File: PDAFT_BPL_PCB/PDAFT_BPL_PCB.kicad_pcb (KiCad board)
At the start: 2 copper layers, 63.4 x 87.5 mm, 18 parts

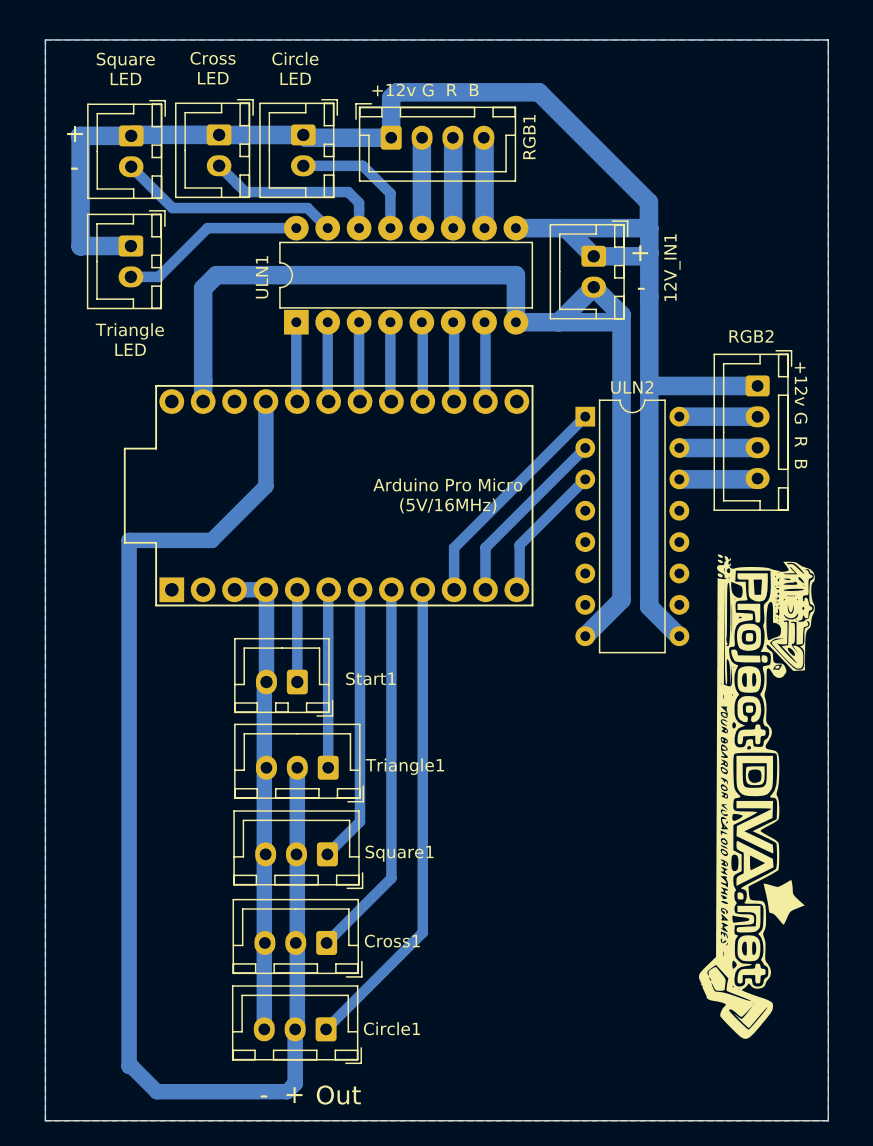
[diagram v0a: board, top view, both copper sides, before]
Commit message: Update PCB
Update PCB to make fast write to registers in interruptions when received LEDs data by UART
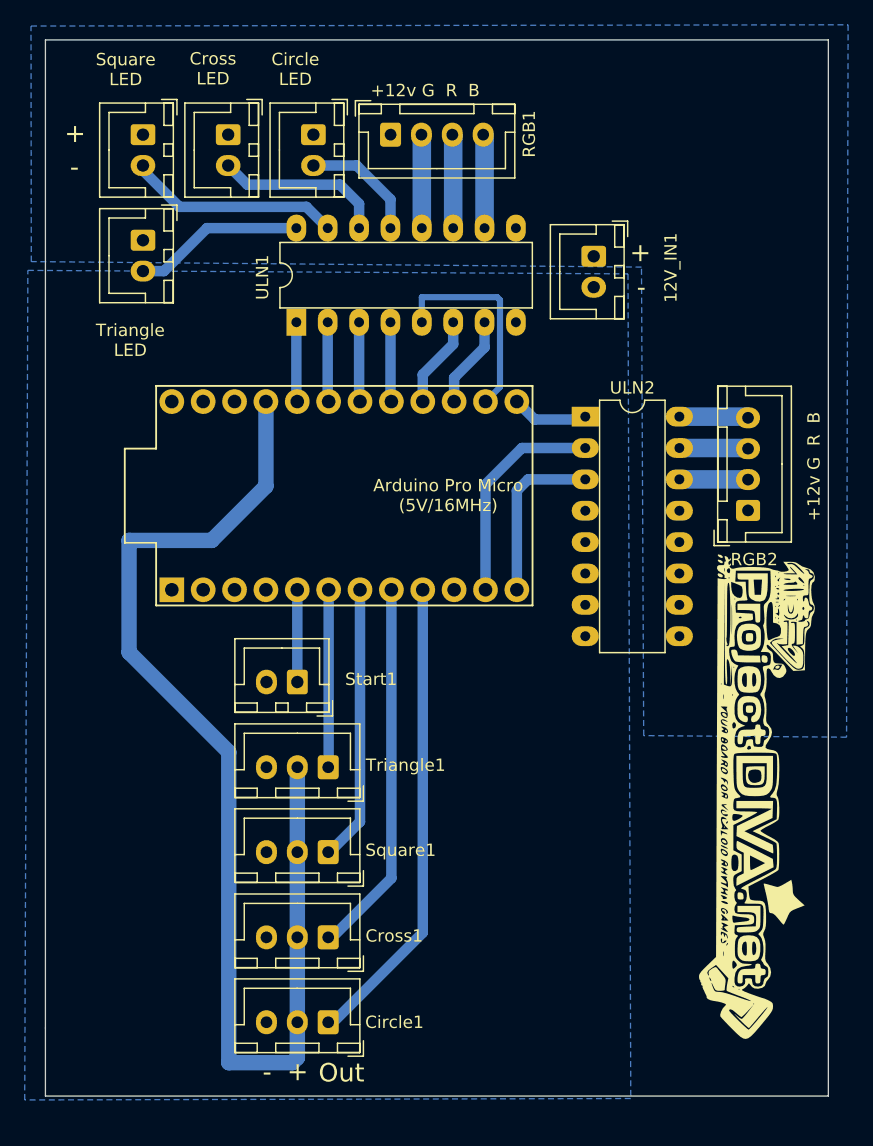
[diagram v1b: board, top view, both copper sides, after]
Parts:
- moved RGB2 10.1 mm to (158.5, 68.6), turned to 90 degrees
- moved G*** 2.63 mm to (153.6, 96.1)
- moved TRIANGLE_LED1 1.08 mm to (109.5, 46.7)
- moved SQUARE_LED1 0.96 mm to (109.5, 38.1)
- moved CIRCLE_LED1 0.82 mm to (123.3, 38.1)
- moved CROSS_LED1 0.74 mm to (116.4, 38.1)
- moved Circle1 0.60 mm to (124.5, 110.0)
- moved Cross1 0.47 mm to (124.5, 103.2)
- moved RGB1 0.25 mm to (129.6, 38.1)
- moved Square1 0.19 mm to (124.5, 96.2)
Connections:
- ProMicro1 pad 1: Net-(ProMicro1-Pad1) -> (no net)
- ProMicro1 pad 10: Net-(ProMicro1-Pad10) -> (no net)
- ProMicro1 pad 2: Net-(ProMicro1-Pad2) -> (no net)
- ProMicro1 pad 22: Net-(ProMicro1-Pad22) -> (no net)
- ProMicro1 pad 24: Net-(ProMicro1-Pad24) -> (no net)
- ULN1 pad 5: Net-(ProMicro1-Pad16) -> Net-(ProMicro1-Pad14)
- ULN1 pad 6: Net-(ProMicro1-Pad15) -> Net-(ProMicro1-Pad16)
- ULN1 pad 7: Net-(ProMicro1-Pad14) -> Net-(ProMicro1-Pad15)
- ULN2 pad 1: Net-(ProMicro1-Pad10) -> Net-(ProMicro1-Pad13)
- ULN2 pad 10: Net-(ULN2-Pad10) -> (no net)
- ULN2 pad 11: Net-(ULN2-Pad11) -> (no net)
- ULN2 pad 12: Net-(ULN2-Pad12) -> (no net)
- ULN2 pad 13: Net-(ULN2-Pad13) -> (no net)
- ULN2 pad 14: Net-(RGB2-Pad4) -> Net-(RGB2-Pad2)
- ULN2 pad 16: Net-(RGB2-Pad2) -> Net-(RGB2-Pad4)
- ULN2 pad 4: Net-(ULN2-Pad4) -> (no net)
- ULN2 pad 5: Net-(ULN2-Pad5) -> (no net)
- ULN2 pad 6: Net-(ULN2-Pad6) -> (no net)
- ULN2 pad 7: Net-(ULN2-Pad7) -> (no net)
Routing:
- net Net-(12V_IN1-Pad1): track 130.0 -> 0.00 mm
- net Net-(12V_IN1-Pad2): track 120.2 -> 0.31 mm
- net Net-(ProMicro1-Pad10): track 18.6 -> 0.00 mm
- net Net-(ProMicro1-Pad14): track 6.46 -> 17.3 mm
- net Net-(Circle1-Pad2): track 103.0 -> 94.8 mm
- net Net-(ProMicro1-Pad13): track 0.00 -> 6.24 mm
- net Net-(ProMicro1-Pad11): track 15.0 -> 17.8 mm
- net Net-(ProMicro1-Pad12): track 11.2 -> 13.9 mm
- net Net-(TRIANGLE_LED1-Pad2): track 15.1 -> 13.9 mm
- net Net-(ProMicro1-Pad16): track 6.46 -> 7.55 mm
- net Net-(CIRCLE_LED1-Pad2): track 10.8 -> 9.70 mm
- net Net-(ProMicro1-Pad15): track 6.46 -> 7.45 mm
- net Net-(RGB2-Pad2): track 6.36 -> 5.59 mm
- net Net-(CROSS_LED1-Pad2): track 14.6 -> 13.9 mm
- net Net-(RGB2-Pad4): track 6.38 -> 5.62 mm
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- added copper zone on B.Cu, net Net-(12V_IN1-Pad1)
- removed copper zone on B.Cu, net (none)
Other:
- board size 63.4 x 87.5 mm -> 63.4 x 85.5 mm

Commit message: Update of PCB and firmware
Updated PCB to have possibility to connect USB-TTL converter to use interuption in serial connection (program for it will be soon completed with various variants of use, now only SerialEvent1() interuption)
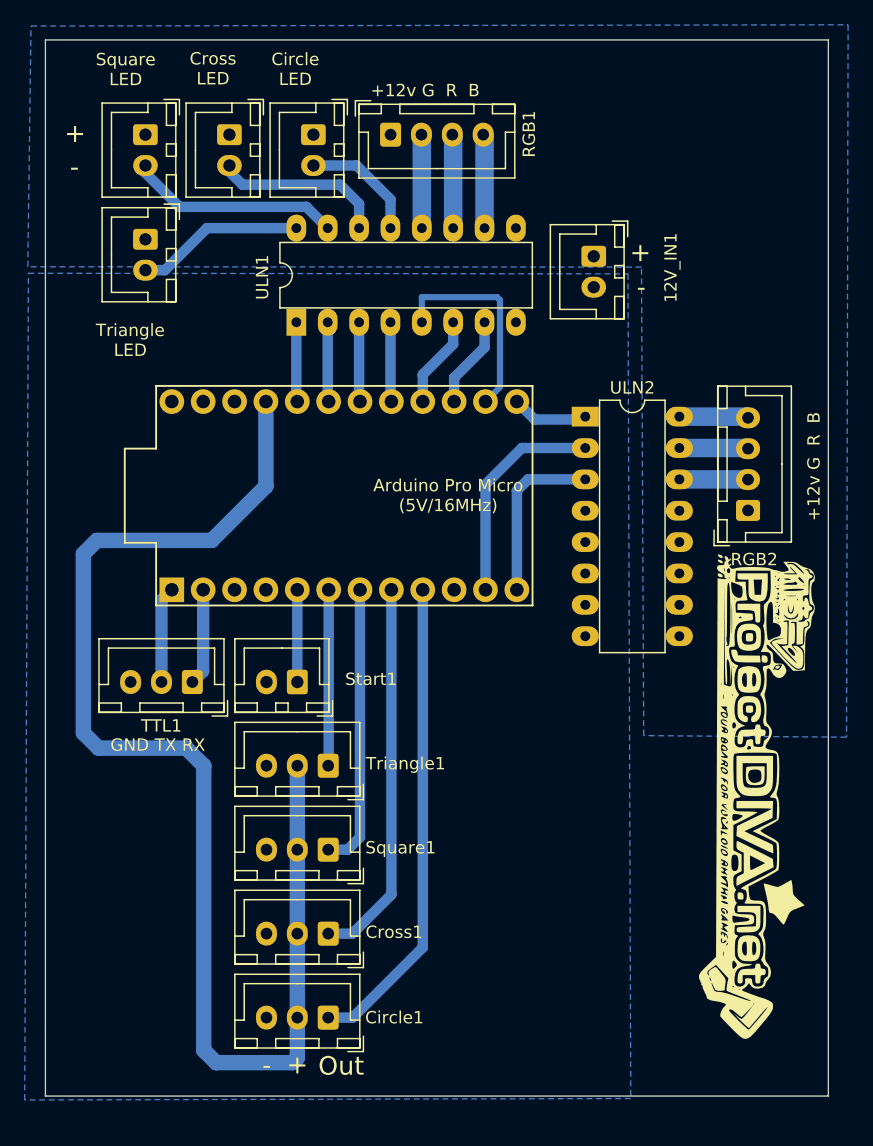
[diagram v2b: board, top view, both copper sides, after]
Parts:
- added TTL1: TTL_Conn_01x03, Connector_JST:JST_XH_B3B-XH-A_1x03_P2.50mm_Vertical, F.Cu at (113.5, 82.5)
- moved Circle1 0.38 mm to (124.5, 109.7)
- moved Cross1 0.30 mm to (124.5, 102.8)
- moved TRIANGLE_LED1 0.21 mm to (109.7, 46.6)
- moved SQUARE_LED1 0.20 mm to (109.7, 38.1)
- moved Square1 0.20 mm to (124.5, 96.0)
- moved Triangle1 0.12 mm to (124.5, 89.2)
- moved CROSS_LED1 0.10 mm to (116.5, 38.1)
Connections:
- ProMicro1 pad 1: (no net) -> Net-(TTL1-Pad2)
- ProMicro1 pad 10: (no net) -> unconnected-(ProMicro1-Pad10)
- ProMicro1 pad 2: (no net) -> Net-(TTL1-Pad1)
- ProMicro1 pad 22: (no net) -> unconnected-(ProMicro1-Pad22)
- ProMicro1 pad 24: (no net) -> unconnected-(ProMicro1-Pad24)
- ULN2 pad 10: (no net) -> unconnected-(ULN2-Pad10)
- ULN2 pad 11: (no net) -> unconnected-(ULN2-Pad11)
- ULN2 pad 12: (no net) -> unconnected-(ULN2-Pad12)
- ULN2 pad 13: (no net) -> unconnected-(ULN2-Pad13)
- ULN2 pad 4: (no net) -> unconnected-(ULN2-Pad4)
- ULN2 pad 5: (no net) -> unconnected-(ULN2-Pad5)
- ULN2 pad 6: (no net) -> unconnected-(ULN2-Pad6)
- ULN2 pad 7: (no net) -> unconnected-(ULN2-Pad7)
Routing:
- net Net-(Circle1-Pad2): track 94.8 -> 104.1 mm
- net Net-(TTL1-Pad1): track 0.00 -> 7.83 mm
- net Net-(TTL1-Pad2): track 0.00 -> 7.82 mm
- net Net-(Cross1-Pad1): track 30.5 -> 31.4 mm
- net Net-(Circle1-Pad1): track 38.4 -> 39.4 mm
- net Net-(ProMicro1-Pad7): track 22.4 -> 23.1 mm
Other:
- board text added: "GND TX RX"

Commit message: Added +5v from TTL to use if needed
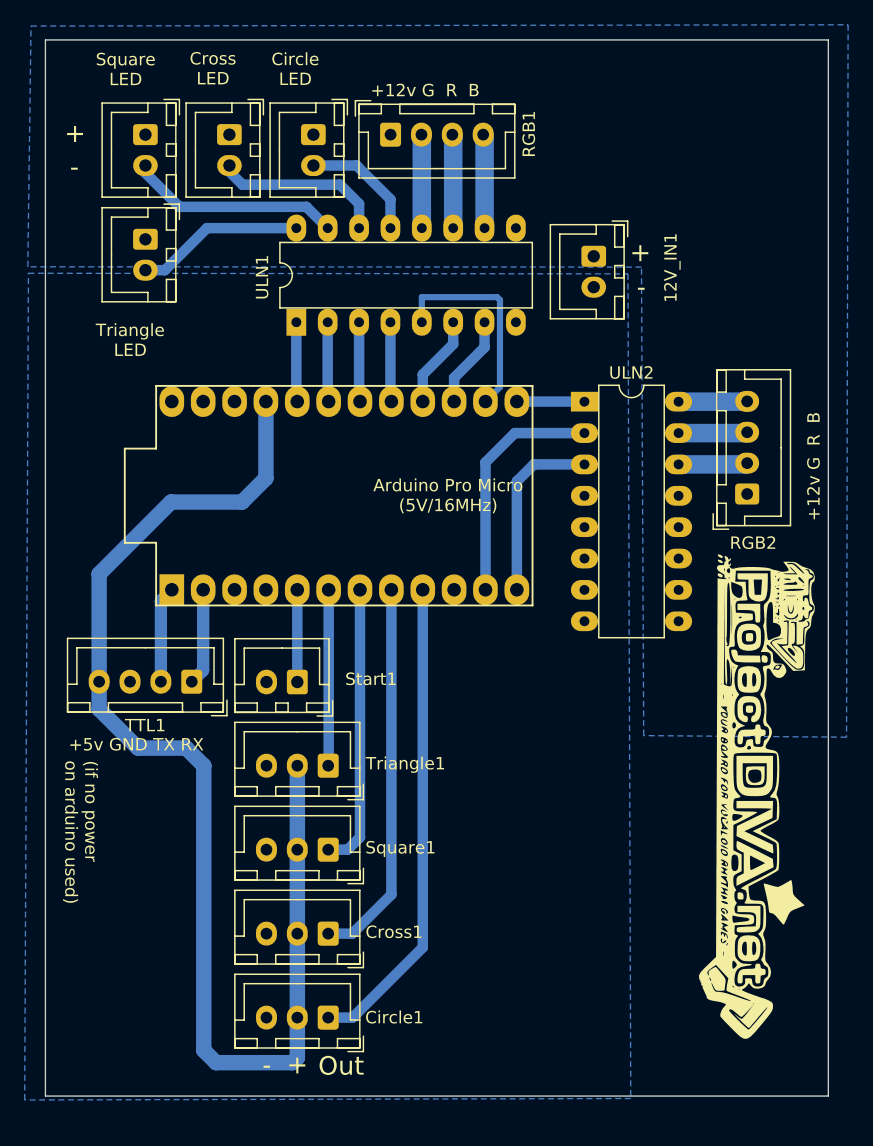
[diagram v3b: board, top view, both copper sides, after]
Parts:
- TTL1: value TTL_Conn_01x03 -> Conn_01x04; footprint Connector_JST:JST_XH_B3B-XH-A_1x03_P2.50mm_Vertical -> Connector_JST:JST_XH_B4B-XH-A_1x04_P2.50mm_Vertical
- moved RGB2 1.33 mm to (158.4, 67.2)
- moved ULN2 1.21 mm to (145.2, 59.8)
- moved TTL1 0.06 mm to (113.5, 82.5)
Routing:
- net Net-(Circle1-Pad2): track 104.1 -> 99.0 mm
- net Net-(ProMicro1-Pad11): track 17.8 -> 19.3 mm
- net Net-(ProMicro1-Pad12): track 13.9 -> 14.8 mm
- net Net-(ProMicro1-Pad13): track 6.24 -> 5.48 mm
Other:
- board text added: "(if no power on arduino used)"
- board text added: "+5v GND TX RX"
- board text removed: "GND TX RX"

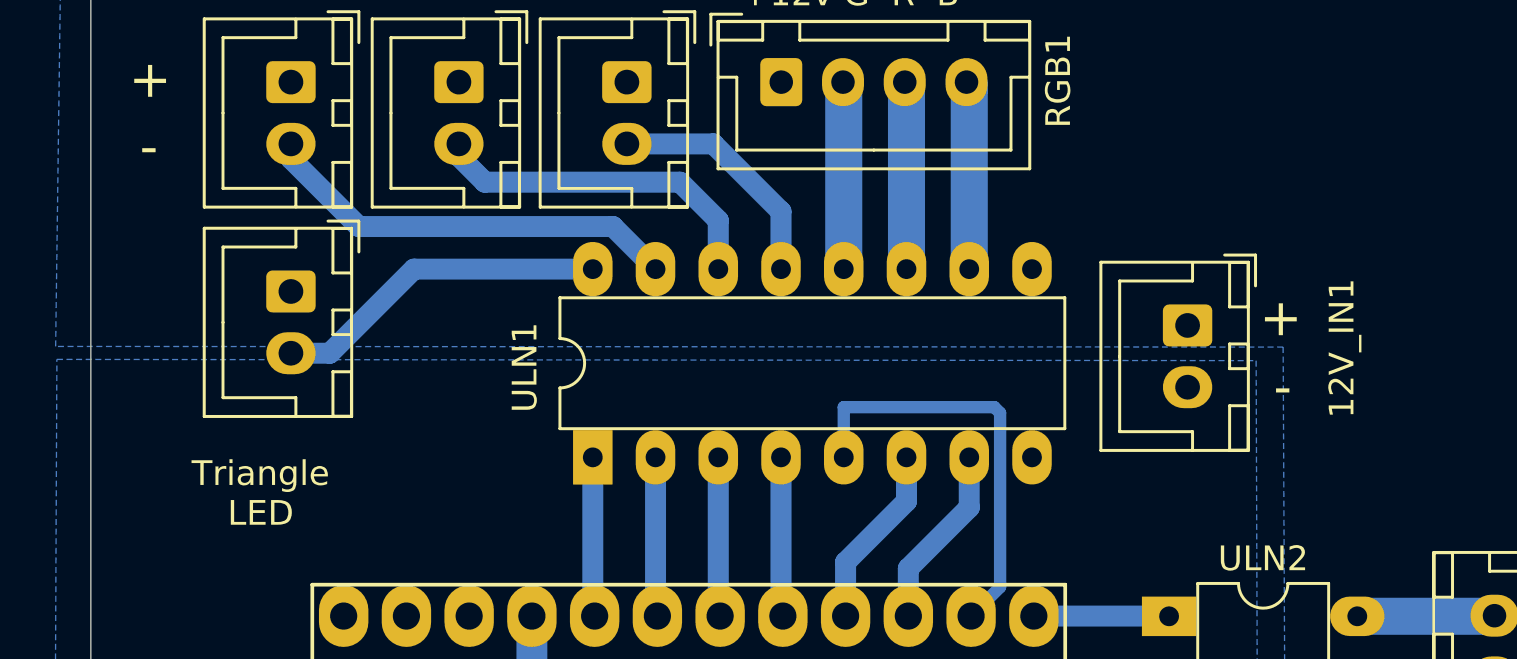
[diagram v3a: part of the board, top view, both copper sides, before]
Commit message: Changing 12vin JST XH2 to XH4
Changing 12Vin JST XH2 to XH4 because of possible current rating limits 3A, so better to parallelize 12Vin to avoid problems with it
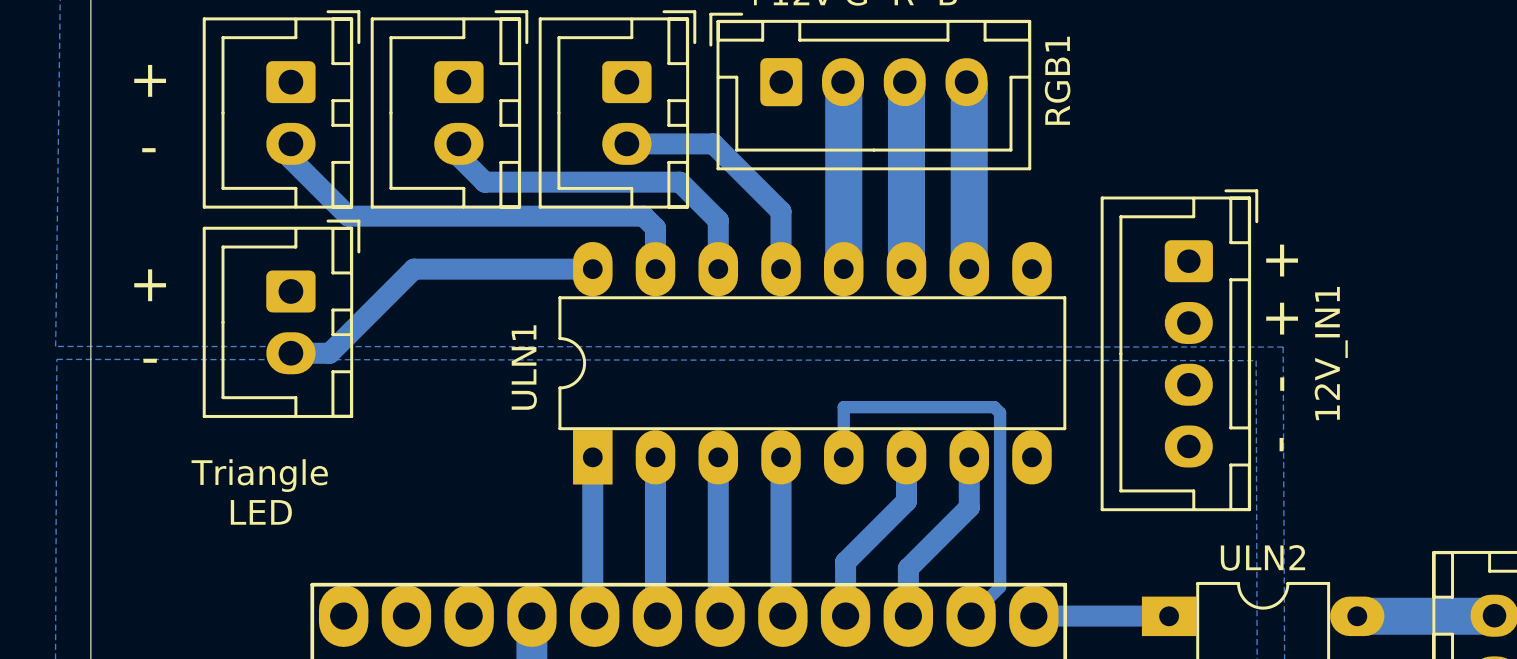
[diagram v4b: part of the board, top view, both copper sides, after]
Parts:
- 12V_IN1: footprint Connector_JST:JST_XH_B2B-XH-A_1x02_P2.50mm_Vertical -> Connector_JST:JST_XH_B4B-XH-A_1x04_P2.50mm_Vertical
- moved 12V_IN1 2.60 mm to (146.1, 45.4)
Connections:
- 12V_IN1 pad 1: Net-(12V_IN1-Pad1) -> Net-(CIRCLE_LED1-Pad1)
- 12V_IN1 pad 2: Net-(12V_IN1-Pad2) -> Net-(CIRCLE_LED1-Pad1)
- CIRCLE_LED1 pad 1: Net-(12V_IN1-Pad1) -> Net-(CIRCLE_LED1-Pad1)
- CROSS_LED1 pad 1: Net-(12V_IN1-Pad1) -> Net-(CIRCLE_LED1-Pad1)
- Circle1 pad 3: Net-(12V_IN1-Pad2) -> Net-(Circle1-Pad3)
- Cross1 pad 3: Net-(12V_IN1-Pad2) -> Net-(Circle1-Pad3)
- ProMicro1 pad 23: Net-(12V_IN1-Pad2) -> Net-(Circle1-Pad3)
- ProMicro1 pad 3: Net-(12V_IN1-Pad2) -> Net-(Circle1-Pad3)
- ProMicro1 pad 4: Net-(12V_IN1-Pad2) -> Net-(Circle1-Pad3)
- RGB1 pad 1: Net-(12V_IN1-Pad1) -> Net-(CIRCLE_LED1-Pad1)
- RGB2 pad 1: Net-(12V_IN1-Pad1) -> Net-(CIRCLE_LED1-Pad1)
- SQUARE_LED1 pad 1: Net-(12V_IN1-Pad1) -> Net-(CIRCLE_LED1-Pad1)
- Square1 pad 3: Net-(12V_IN1-Pad2) -> Net-(Circle1-Pad3)
- Start1 pad 2: Net-(12V_IN1-Pad2) -> Net-(Circle1-Pad3)
- TRIANGLE_LED1 pad 1: Net-(12V_IN1-Pad1) -> Net-(CIRCLE_LED1-Pad1)
- TTL1 pad 3: Net-(12V_IN1-Pad2) -> Net-(Circle1-Pad3)
- Triangle1 pad 3: Net-(12V_IN1-Pad2) -> Net-(Circle1-Pad3)
- ULN1 pad 8: Net-(12V_IN1-Pad2) -> Net-(Circle1-Pad3)
- ULN1 pad 9: Net-(12V_IN1-Pad1) -> Net-(CIRCLE_LED1-Pad1)
- ULN2 pad 8: Net-(12V_IN1-Pad2) -> Net-(Circle1-Pad3)
- ULN2 pad 9: Net-(12V_IN1-Pad1) -> Net-(CIRCLE_LED1-Pad1)
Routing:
- net Net-(SQUARE_LED1-Pad2): track 17.6 -> 18.6 mm
- added copper zone on B.Cu, net Net-(CIRCLE_LED1-Pad1)
- added copper zone on B.Cu, net Net-(Circle1-Pad3)
- removed copper zone on B.Cu, net Net-(12V_IN1-Pad1)
- removed copper zone on B.Cu, net Net-(12V_IN1-Pad2)
